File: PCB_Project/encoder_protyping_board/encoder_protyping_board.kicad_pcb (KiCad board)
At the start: 2 copper layers, 22 x 21.6 mm, 13 parts, among them J1 Conn_02x04_Counter_Clockwise, J2 Conn_01x02_Pin, J3 Conn_01x03_Pin

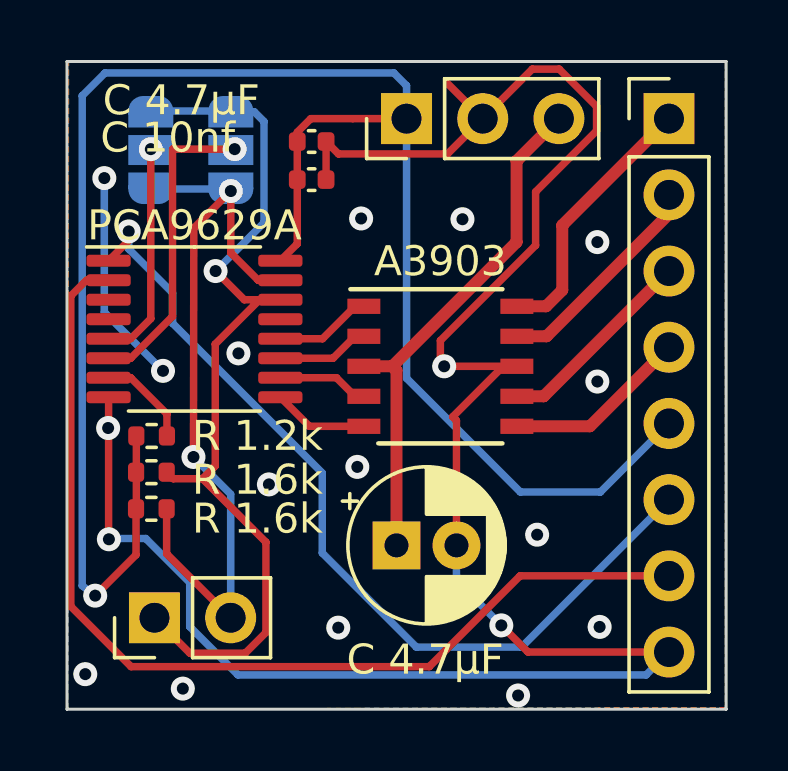
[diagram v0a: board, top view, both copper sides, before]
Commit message: lock removed and updated to kicad 8
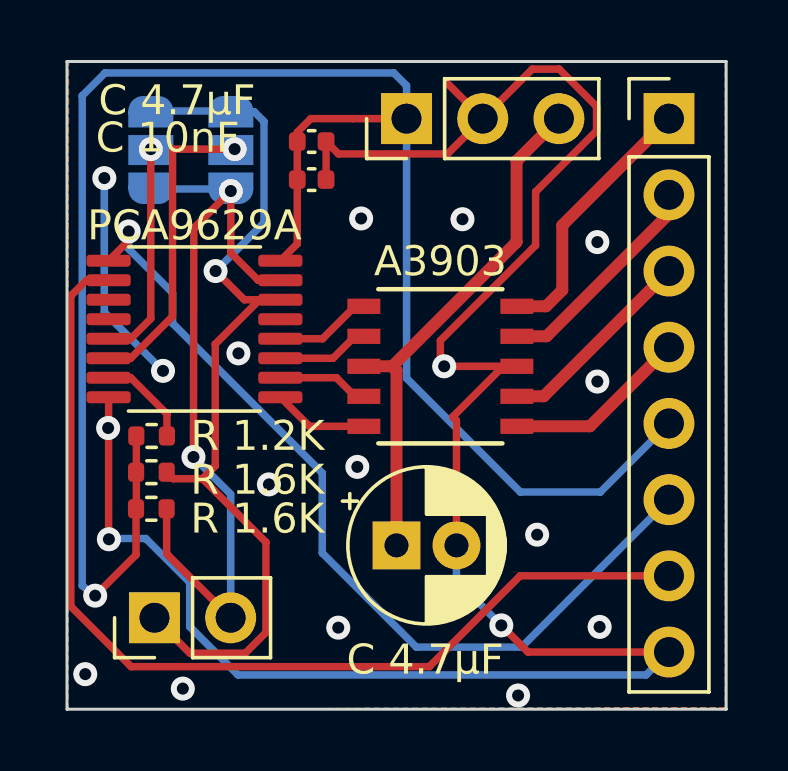
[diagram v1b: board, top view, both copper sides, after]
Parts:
- C 10nF: renamed from C 10nf
- C 4.7µF: renamed from C 4.7μF (x2)
- R 1.2K: renamed from R 1.2k
- R 1.6K: renamed from R 1.6k (x2)

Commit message: bunch of things
added to the rear silkscreen
moved I2C header to edge of board
rerouted lines so no signals ran around the edge of the board
beefed up ground to A3903
made sure ground was around all edges of the board
cleaned up the 5v runs
added pin 1 markers for the 2 ICs to front silkscreen
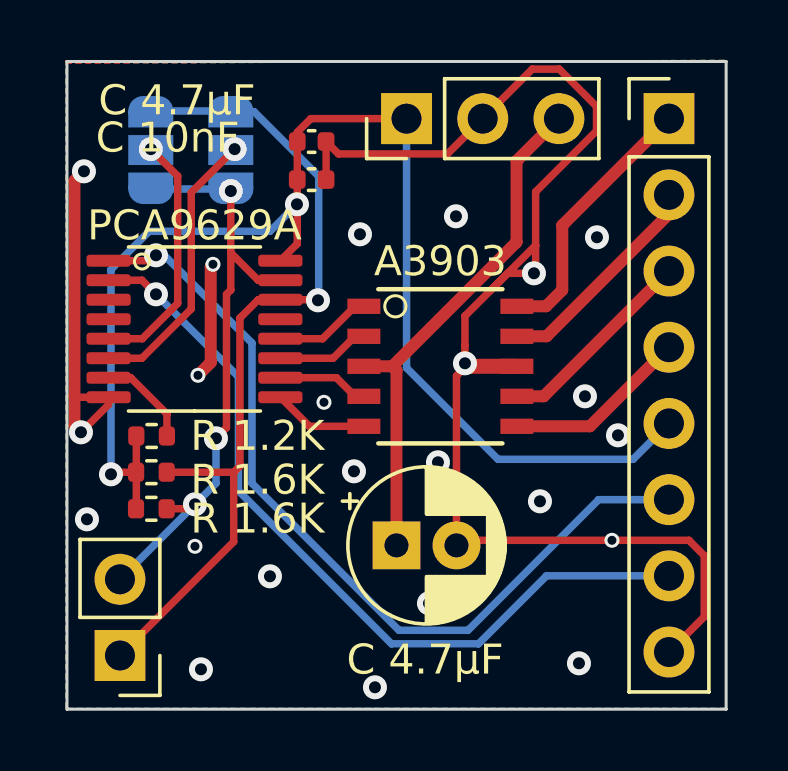
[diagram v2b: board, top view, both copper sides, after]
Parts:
- moved J2 1.70 mm to (57.9, 35.0), turned to 180 degrees
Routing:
- net +5V: track 64.2 -> 44.4 mm, vias 1 -> 2
- net GND: track 77.3 -> 60.7 mm, vias 19 -> 23
- net Net-(J1-Pin_7): track 33.9 -> 26.9 mm, vias 0 -> 1
- net I2C_SDA: track 26.7 -> 20.2 mm, vias 2 -> 3
- net I2C_SCL: track 31.4 -> 28.6 mm
- net Net-(J1-Pin_6): track 29.6 -> 28.5 mm
- net Net-(JP1-C): track 10.4 -> 9.36 mm
- net Net-(JP2-C): track 7.33 -> 8.30 mm
- net +12V: track 18.3 -> 17.5 mm
- net Net-(J1-Pin_2): track 7.39 -> 6.76 mm
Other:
- board text added: "I2C Stepper Driver-E D Verbeek STARR 2024"
